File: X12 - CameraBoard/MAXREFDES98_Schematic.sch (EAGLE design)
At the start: 29 parts, among them U1 MB110S-TP, U2 MB110S-TP, U3 MAX5969AETB+, U4 MAX17503ATP+

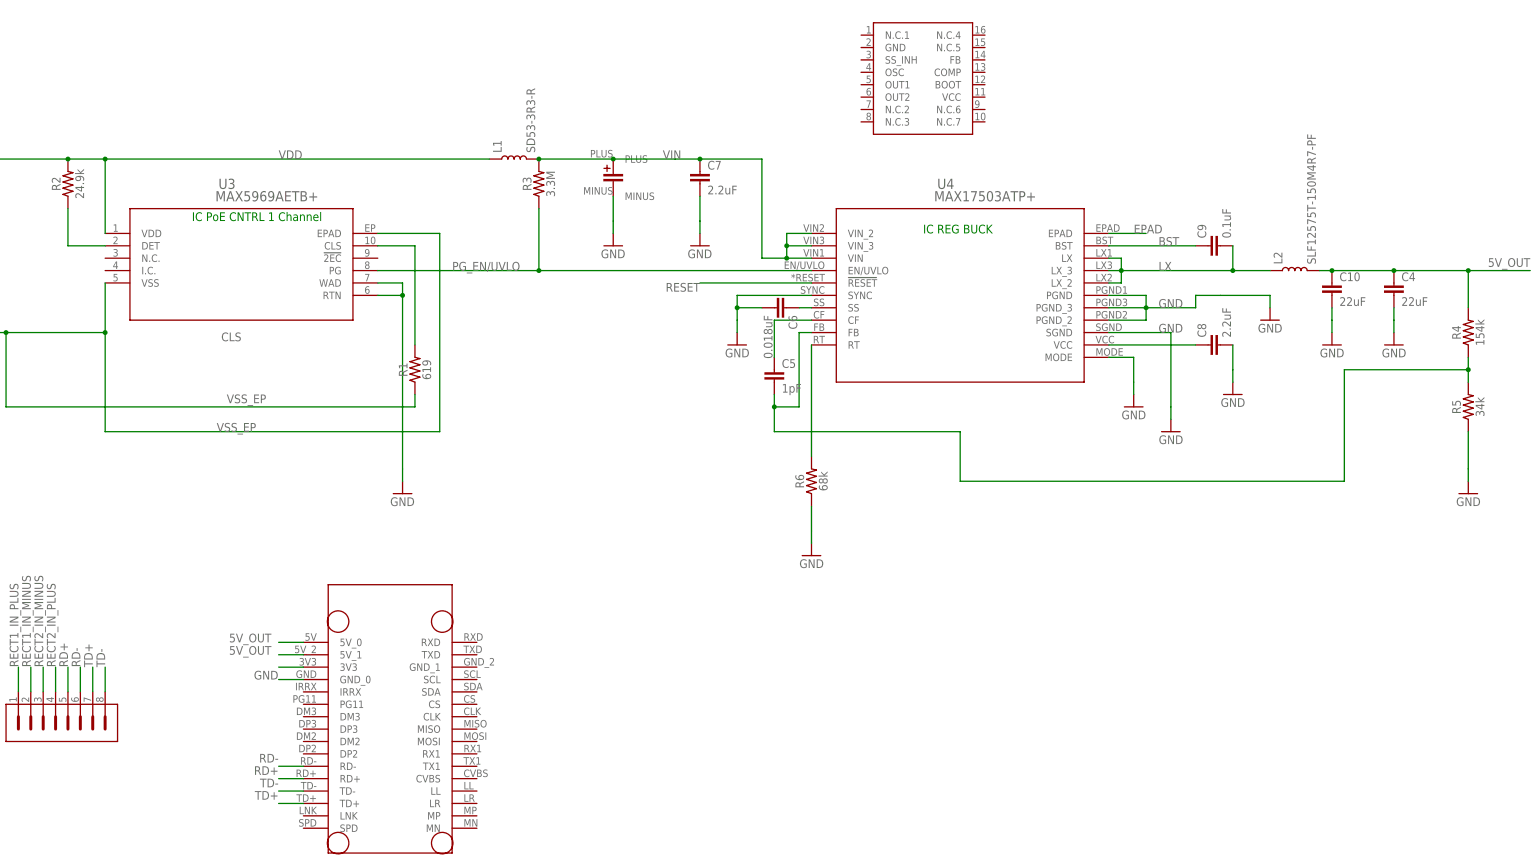
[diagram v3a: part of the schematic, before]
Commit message: Added new buck converter, plus supporting circuitry
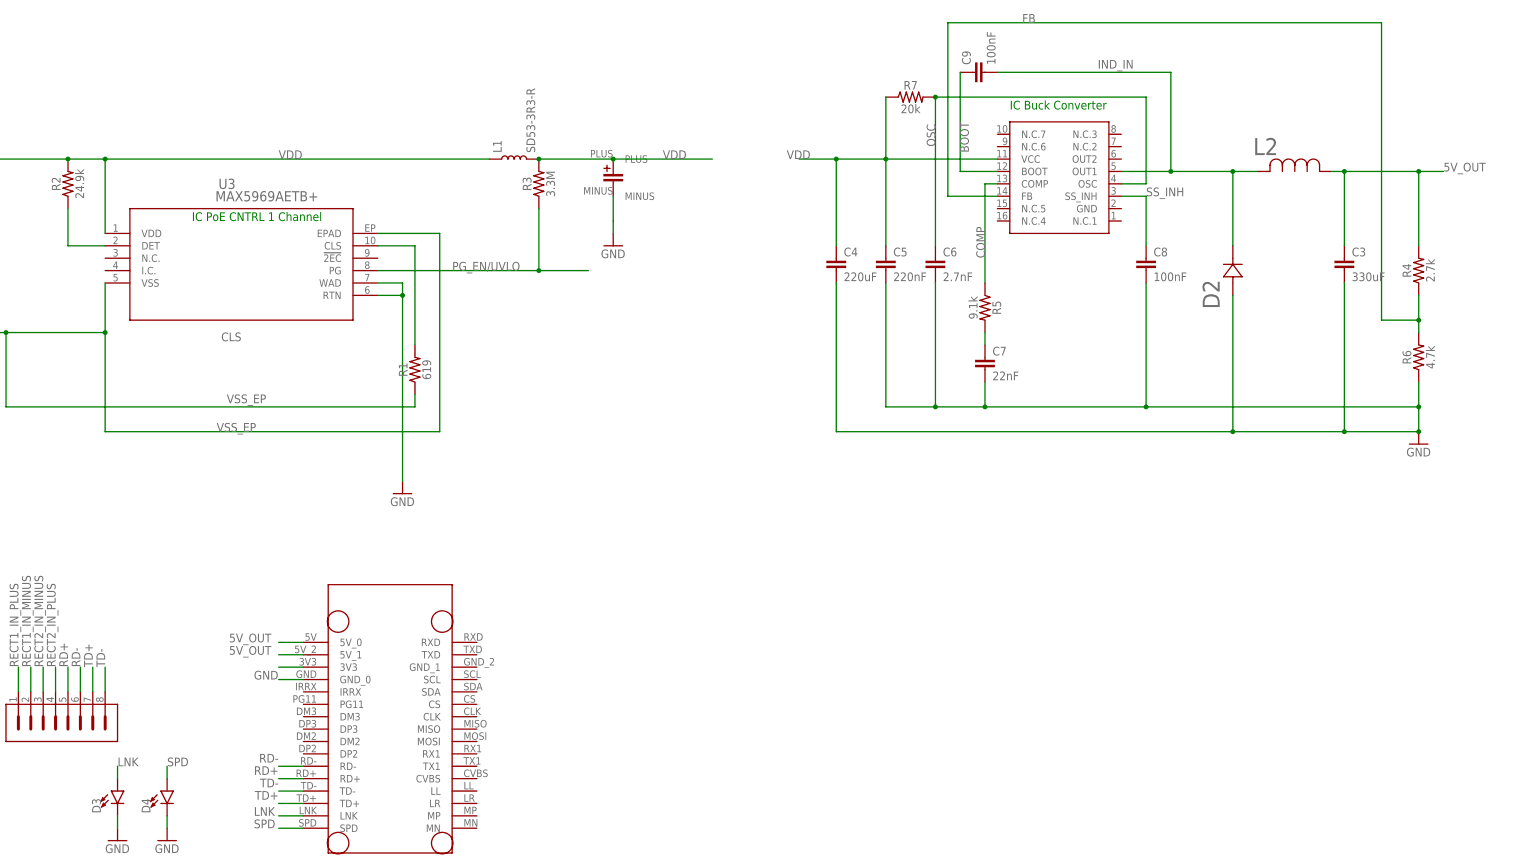
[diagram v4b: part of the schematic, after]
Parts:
- removed C10: 22uF, SparkFun-Capacitors:10UF-1210-50V-20%
- removed U4: MAX17503ATP+, MAX17503ATP+:MAX17503ATP+
- added C3: 330uF, SparkFun-Capacitors:4.7UF0603
- added D2: STPS3L60USMB_STM-M, Camera_Board_Parts_09_30_2020:STPS3L60USMB_STM-M
- added D3, D4: (no value), SparkFun-LED:LED-FKIT-1206
- added R7: 20k, SparkFun-Resistors:0.22OHM-0805-1/4W-1%
- C4: value 22uF -> 220uF; device SparkFun-Capacitors:10UF-1210-50V-20% -> SparkFun-Capacitors:4.7UF0603
- C5: value 1pF -> 220nF
- C6: value 0.018uF -> 2.7nF; device SparkFun-Capacitors:0.1UF-0603-25V-(+80/-20%) -> SparkFun-Capacitors:4.7UF0603
- C7: value 2.2uF -> 22nF; device SparkFun-Capacitors:10UF-1210-50V-20% -> SparkFun-Capacitors:4.7UF0603
- C8: value 2.2uF -> 100nF; device SparkFun-Capacitors:0.1UF-0603-25V-(+80/-20%) -> SparkFun-Capacitors:4.7UF0603
- C9: value 0.1uF -> 100nF; device SparkFun-Capacitors:0.1UF-0603-25V-(+80/-20%) -> SparkFun-Capacitors:4.7UF0603
- L2: value SLF12575T-150M4R7-PF -> SRR1806-151M; device SLF12575T-150M4R7-PF:SLF12575T-150M4R7-PF -> Camera_Board_Parts_09_30_2020:SRR1806-151M
- R4: value 154k -> 2.7k; device SparkFun-Resistors:0.05OHM-0603-1/5W-1% -> SparkFun-Resistors:0.22OHM-0805-1/4W-1%
- R5: value 34k -> 9.1k; device SparkFun-Resistors:0.05OHM-0603-1/5W-1% -> SparkFun-Resistors:0.22OHM-0805-1/4W-1%
- R6: value 68k -> 4.7k; device SparkFun-Resistors:RESISTOR0603 -> SparkFun-Resistors:0.22OHM-0805-1/4W-1%
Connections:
- removed net BST: C9.1, U4.BST
- removed net CF: C5.1, U4.CF
- removed net EPAD: U4.EPAD
- removed net LX: C9.2, L2.1, U4.LX, U4.LX_2, U4.LX_3
- removed net RESET: U4.!RESET
- removed net RT: R6.2, U4.RT
- removed net SS: C6.1, U4.SS
- removed net VCC: C8.1, U4.VCC
- removed net VIN: C2.PLUS, C7.1, L1.2, R3.2, U4.VIN, U4.VIN_2, U4.VIN_3
- new net BOOT: C9.1, U$1.BOOT
- new net COMP: R5.1, U$1.COMP
- new net IND_IN: C9.2, D2.1, L2.2, U$1.OUT1
- new net LNK: D3.A, U$2.LNK
- new net N$6: C7.1, R5.2
- new net OSC: C6.1, R7.2, U$1.OSC
- new net SPD: D4.A, U$2.SPD
- new net SS_INH: C8.1, U$1.SS_INH
- net 5V_OUT: now also C3.1, L2.1; no longer C10.1, C4.1, L2.2
- net FB: now also R6.2, U$1.FB; no longer C5.2, R5.2, U4.FB
- net GND: now also C3.2, C5.2, D2.2, D3.C, D4.C; no longer C10.2, R5.1, U4.MODE, U4.PGND, U4.PGND_2, U4.PGND_3, U4.SGND, U4.SYNC
- net PG_EN/UVLO: no longer U4.EN/UVLO
- net VDD: now also C2.PLUS, C4.1, C5.1, L1.2, R3.2, R7.1, U$1.VCC
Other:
- note added: "IC Buck Converter"
- note removed: "IC REG BUCK"
- moved on the sheet: C4, C5, C6, C7, C8, C9, R4, R5, R6
